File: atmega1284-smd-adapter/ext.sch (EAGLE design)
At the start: 5 parts

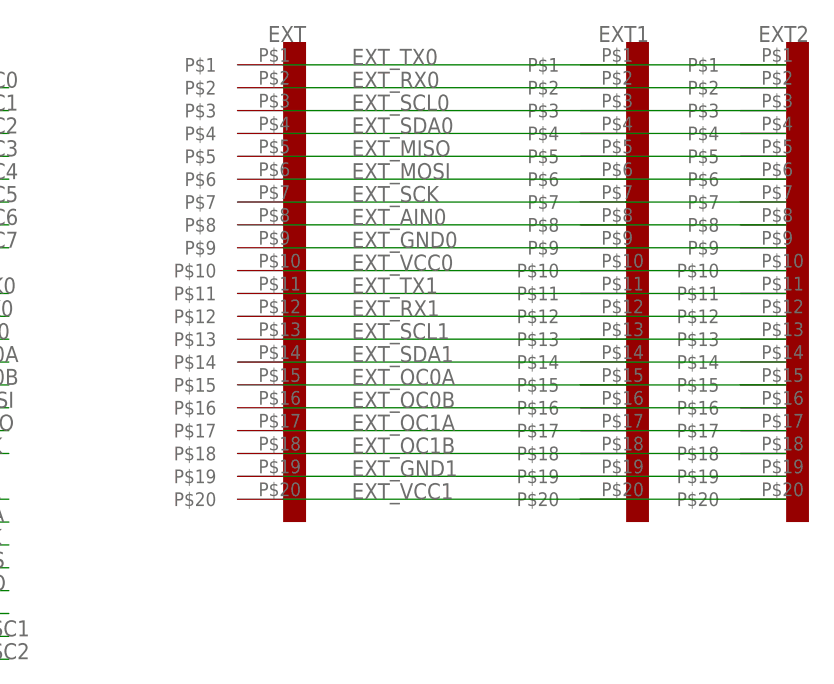
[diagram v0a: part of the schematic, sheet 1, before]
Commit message: [mk2 adapter split]
	- split the mk2-ext adapters into the actual mk2 extension board and
	  the atmega1284 smd adapter
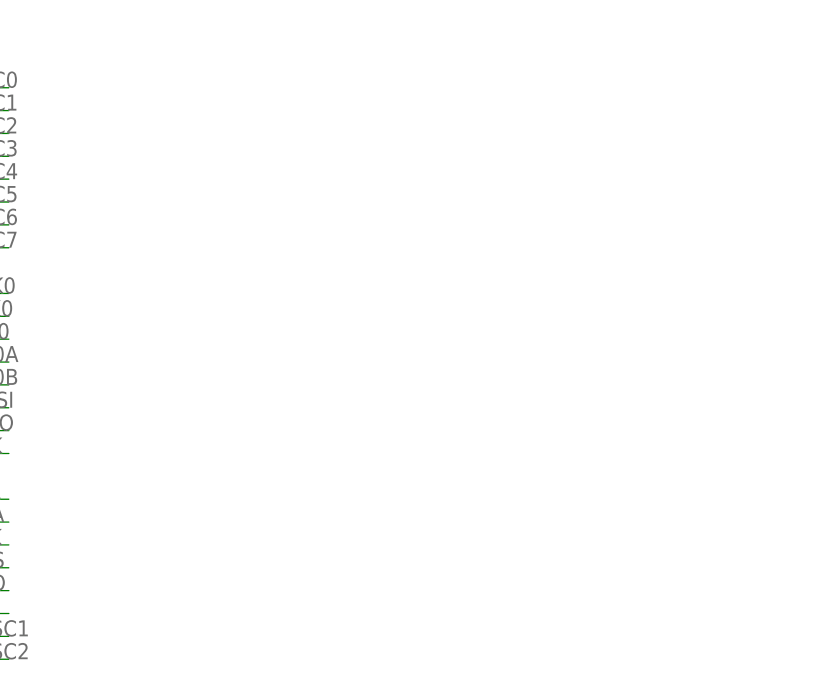
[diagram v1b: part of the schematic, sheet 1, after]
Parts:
- removed EXT, EXT1, EXT2: CON_DIL_20, connector:CON_DIL_20
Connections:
- removed net EXT_AIN0: EXT.P$8, EXT1.P$8, EXT2.P$8
- removed net EXT_GND0: EXT.P$9, EXT1.P$9, EXT2.P$9
- removed net EXT_GND1: EXT.P$19, EXT1.P$19, EXT2.P$19
- removed net EXT_MISO: EXT.P$5, EXT1.P$5, EXT2.P$5
- removed net EXT_MOSI: EXT.P$6, EXT1.P$6, EXT2.P$6
- removed net EXT_OC0A: EXT.P$15, EXT1.P$15, EXT2.P$15
- removed net EXT_OC0B: EXT.P$16, EXT1.P$16, EXT2.P$16
- removed net EXT_OC1A: EXT.P$17, EXT1.P$17, EXT2.P$17
- removed net EXT_OC1B: EXT.P$18, EXT1.P$18, EXT2.P$18
- removed net EXT_RX0: EXT.P$2, EXT1.P$2, EXT2.P$2
- removed net EXT_RX1: EXT.P$12, EXT1.P$12, EXT2.P$12
- removed net EXT_SCK: EXT.P$7, EXT1.P$7, EXT2.P$7
- removed net EXT_SCL0: EXT.P$3, EXT1.P$3, EXT2.P$3
- removed net EXT_SCL1: EXT.P$13, EXT1.P$13, EXT2.P$13
- removed net EXT_SDA0: EXT.P$4, EXT1.P$4, EXT2.P$4
- removed net EXT_SDA1: EXT.P$14, EXT1.P$14, EXT2.P$14
- removed net EXT_TX0: EXT.P$1, EXT1.P$1, EXT2.P$1
- removed net EXT_TX1: EXT.P$11, EXT1.P$11, EXT2.P$11
- removed net EXT_VCC0: EXT.P$10, EXT1.P$10, EXT2.P$10
- removed net EXT_VCC1: EXT.P$20, EXT1.P$20, EXT2.P$20
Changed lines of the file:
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@@
 <part name="GND7" library="supply1" library_urn="urn:adsk.eagle:library:371" deviceset="GND" device=""/>
 <part name="P+5" library="supply1" library_urn="urn:adsk.eagle:library:371" deviceset="VCC" device=""/>
-<part name="EXT" library="connector" deviceset="CON_DIL_20" device=""/>
 <part name="P+1" library="supply1" library_urn="urn:adsk.eagle:library:371" deviceset="VCC" device=""/>
 <part name="GND1" library="supply1" library_urn="urn:adsk.eagle:library:371" deviceset="GND" device=""/>
-<part name="EXT1" library="connector" deviceset="CON_DIL_20" device=""/>
-<part name="EXT2" library="connector" deviceset="CON_DIL_20" device=""/>
 </parts>
 <sheets>
@@
 <attribute name="VALUE" x="58.42" y="132.08" size="1.778" layer="96"/>
 </instance>
-<instance part="EXT" gate="G$1" x="152.4" y="109.22" smashed="yes">
-<attribute name="NAME" x="154.94" y="132.08" size="1.778" layer="95" rot="MR0"/>
-</instance>
 <instance part="P+1" gate="VCC" x="-33.02" y="132.08" smashed="yes">
 <attribute name="VALUE" x="-30.48" y="129.54" size="1.778" layer="96"/>
@@
 <instance part="GND1" gate="1" x="-30.48" y="30.48" smashed="yes">
 <attribute name="VALUE" x="-33.02" y="27.94" size="1.778" layer="96"/>
-</instance>
-<instance part="EXT1" gate="G$1" x="190.5" y="109.22" smashed="yes">
-<attribute name="NAME" x="193.04" y="132.08" size="1.778" layer="95" rot="MR0"/>
-</instance>
-<instance part="EXT2" gate="G$1" x="208.28" y="109.22" smashed="yes">
-<attribute name="NAME" x="210.82" y="132.08" size="1.778" layer="95" rot="MR0"/>
 </instance>
 </instances>
@@
 </segment>
 </net>
-<net name="EXT_TX0" class="0">
-<segment>
-<pinref part="EXT" gate="G$1" pin="P$1"/>
-<label x="160.02" y="129.54" size="1.778" layer="95"/>
-<wire x1="190.5" y1="129.54" x2="152.4" y2="129.54" width="0.1524" layer="91"/>
-<pinref part="EXT1" gate="G$1" pin="P$1"/>
-<pinref part="EXT2" gate="G$1" pin="P$1"/>
-<wire x1="208.28" y1="129.54" x2="190.5" y2="129.54" width="0.1524" layer="91"/>
-</segment>
-</net>
-<net name="EXT_RX0" class="0">
-<segment>
-<pinref part="EXT" gate="G$1" pin="P$2"/>
-<label x="160.02" y="127" size="1.778" layer="95"/>
-<wire x1="190.5" y1="127" x2="152.4" y2="127" width="0.1524" layer="91"/>
-<pinref part="EXT1" gate="G$1" pin="P$2"/>
-<pinref part="EXT2" gate="G$1" pin="P$2"/>
-<wire x1="208.28" y1="127" x2="190.5" y2="127" width="0.1524" layer="91"/>
-</segment>
-</net>
-<net name="EXT_SCL1" class="0">
-<segment>
-<pinref part="EXT" gate="G$1" pin="P$13"/>
-<label x="160.02" y="99.06" size="1.778" layer="95"/>
-<wire x1="190.5" y1="99.06" x2="152.4" y2="99.06" width="0.1524" layer="91"/>
-<pinref part="EXT1" gate="G$1" pin="P$13"/>
-<pinref part="EXT2" gate="G$1" pin="P$13"/>
-<wire x1="208.28" y1="99.06" x2="190.5" y2="99.06" width="0.1524" layer="91"/>
-</segment>
-</net>
-<net name="EXT_SDA0" class="0">
-<segment>
-<pinref part="EXT" gate="G$1" pin="P$4"/>
-<label x="160.02" y="121.92" size="1.778" layer="95"/>
-<wire x1="190.5" y1="121.92" x2="152.4" y2="121.92" width="0.1524" layer="91"/>
-<pinref part="EXT1" gate="G$1" pin="P$4"/>
-<pinref part="EXT2" gate="G$1" pin="P$4"/>
-<wire x1="208.28" y1="121.92" x2="190.5" y2="121.92" width="0.1524" layer="91"/>
-</segment>
-</net>
-<net name="EXT_MISO" class="0">
-<segment>
-<pinref part="EXT" gate="G$1" pin="P$5"/>
-<label x="160.02" y="119.38" size="1.778" layer="95"/>
-<wire x1="190.5" y1="119.38" x2="152.4" y2="119.38" width="0.1524" layer="91"/>
-<pinref part="EXT1" gate="G$1" pin="P$5"/>
-<pinref part="EXT2" gate="G$1" pin="P$5"/>
-<wire x1="208.28" y1="119.38" x2="190.5" y2="119.38" width="0.1524" layer="91"/>
-</segment>
-</net>
-<net name="EXT_MOSI" class="0">
-<segment>
-<pinref part="EXT" gate="G$1" pin="P$6"/>
-<label x="160.02" y="116.84" size="1.778" layer="95"/>
-<wire x1="190.5" y1="116.84" x2="152.4" y2="116.84" width="0.1524" layer="91"/>
-<pinref part="EXT1" gate="G$1" pin="P$6"/>
-<pinref part="EXT2" gate="G$1" pin="P$6"/>
-<wire x1="208.28" y1="116.84" x2="190.5" y2="116.84" width="0.1524" layer="91"/>
-</segment>
-</net>
-<net name="EXT_SCK" class="0">
-<segment>
-<pinref part="EXT" gate="G$1" pin="P$7"/>
-<label x="160.02" y="114.3" size="1.778" layer="95"/>
-<wire x1="190.5" y1="114.3" x2="152.4" y2="114.3" width="0.1524" layer="91"/>
-<pinref part="EXT1" gate="G$1" pin="P$7"/>
-<pinref part="EXT2" gate="G$1" pin="P$7"/>
-<wire x1="208.28" y1="114.3" x2="190.5" y2="114.3" width="0.1524" layer="91"/>
-</segment>
-</net>
-<net name="EXT_AIN0" class="0">
-<segment>
-<pinref part="EXT" gate="G$1" pin="P$8"/>
-<label x="160.02" y="111.76" size="1.778" layer="95"/>
-<wire x1="190.5" y1="111.76" x2="152.4" y2="111.76" width="0.1524" layer="91"/>
-<pinref part="EXT1" gate="G$1" pin="P$8"/>
-<pinref part="EXT2" gate="G$1" pin="P$8"/>
-<wire x1="208.28" y1="111.76" x2="190.5" y2="111.76" width="0.1524" layer="91"/>
-</segment>
-</net>
-<net name="EXT_GND0" class="0">
-<segment>
-<pinref part="EXT" gate="G$1" pin="P$9"/>
-<label x="160.02" y="109.22" size="1.778" layer="95"/>
-<wire x1="190.5" y1="109.22" x2="152.4" y2="109.22" width="0.1524" layer="91"/>
-<pinref part="EXT1" gate="G$1" pin="P$9"/>
-<pinref part="EXT2" gate="G$1" pin="P$9"/>
-<wire x1="208.28" y1="109.22" x2="190.5" y2="109.22" width="0.1524" layer="91"/>
-</segment>
-</net>
-<net name="EXT_VCC0" class="0">
-<segment>
-<pinref part="EXT" gate="G$1" pin="P$10"/>
-<label x="160.02" y="106.68" size="1.778" layer="95"/>
-<wire x1="190.5" y1="106.68" x2="152.4" y2="106.68" width="0.1524" layer="91"/>
-<pinref part="EXT1" gate="G$1" pin="P$10"/>
-<pinref part="EXT2" gate="G$1" pin="P$10"/>
-<wire x1="208.28" y1="106.68" x2="190.5" y2="106.68" width="0.1524" layer="91"/>
-</segment>
-</net>
-<net name="EXT_TX1" class="0">
-<segment>
-<pinref part="EXT" gate="G$1" pin="P$11"/>
-<label x="160.02" y="104.14" size="1.778" layer="95"/>
-<wire x1="190.5" y1="104.14" x2="152.4" y2="104.14" width="0.1524" layer="91"/>
-<pinref part="EXT1" gate="G$1" pin="P$11"/>
-<pinref part="EXT2" gate="G$1" pin="P$11"/>
-<wire x1="208.28" y1="104.14" x2="190.5" y2="104.14" width="0.1524" layer="91"/>
-</segment>
-</net>
-<net name="EXT_RX1" class="0">
-<segment>
-<pinref part="EXT" gate="G$1" pin="P$12"/>
-<label x="160.02" y="101.6" size="1.778" layer="95"/>
-<wire x1="190.5" y1="101.6" x2="152.4" y2="101.6" width="0.1524" layer="91"/>
-<pinref part="EXT1" gate="G$1" pin="P$12"/>
-<pinref part="EXT2" gate="G$1" pin="P$12"/>
-<wire x1="208.28" y1="101.6" x2="190.5" y2="101.6" width="0.1524" layer="91"/>
-</segment>
-</net>
-<net name="EXT_SCL0" class="0">
-<segment>
-<pinref part="EXT" gate="G$1" pin="P$3"/>
-<label x="160.02" y="124.46" size="1.778" layer="95"/>
-<wire x1="190.5" y1="124.46" x2="152.4" y2="124.46" width="0.1524" layer="91"/>
-<pinref part="EXT1" gate="G$1" pin="P$3"/>
-<pinref part="EXT2" gate="G$1" pin="P$3"/>
-<wire x1="208.28" y1="124.46" x2="190.5" y2="124.46" width="0.1524" layer="91"/>
-</segment>
-</net>
-<net name="EXT_SDA1" class="0">
-<segment>
-<pinref part="EXT" gate="G$1" pin="P$14"/>
-<label x="160.02" y="96.52" size="1.778" layer="95"/>
-<wire x1="190.5" y1="96.52" x2="152.4" y2="96.52" width="0.1524" layer="91"/>
-<pinref part="EXT1" gate="G$1" pin="P$14"/>
-<pinref part="EXT2" gate="G$1" pin="P$14"/>
-<wire x1="208.28" y1="96.52" x2="190.5" y2="96.52" width="0.1524" layer="91"/>
-</segment>
-</net>
-<net name="EXT_OC0A" class="0">
-<segment>
-<pinref part="EXT" gate="G$1" pin="P$15"/>
-<label x="160.02" y="93.98" size="1.778" layer="95"/>
-<wire x1="190.5" y1="93.98" x2="152.4" y2="93.98" width="0.1524" layer="91"/>
-<pinref part="EXT1" gate="G$1" pin="P$15"/>
-<pinref part="EXT2" gate="G$1" pin="P$15"/>
-<wire x1="208.28" y1="93.98" x2="190.5" y2="93.98" width="0.1524" layer="91"/>
-</segment>
-</net>
-<net name="EXT_OC0B" class="0">
-<segment>
-<pinref part="EXT" gate="G$1" pin="P$16"/>
-<label x="160.02" y="91.44" size="1.778" layer="95"/>
-<wire x1="190.5" y1="91.44" x2="152.4" y2="91.44" width="0.1524" layer="91"/>
-<pinref part="EXT1" gate="G$1" pin="P$16"/>
-<pinref part="EXT2" gate="G$1" pin="P$16"/>
-<wire x1="208.28" y1="91.44" x2="190.5" y2="91.44" width="0.1524" layer="91"/>
-</segment>
-</net>
-<net name="EXT_OC1A" class="0">
-<segment>
-<pinref part="EXT" gate="G$1" pin="P$17"/>
-<label x="160.02" y="88.9" size="1.778" layer="95"/>
-<wire x1="190.5" y1="88.9" x2="152.4" y2="88.9" width="0.1524" layer="91"/>
-<pinref part="EXT1" gate="G$1" pin="P$17"/>
-<pinref part="EXT2" gate="G$1" pin="P$17"/>
-<wire x1="208.28" y1="88.9" x2="190.5" y2="88.9" width="0.1524" layer="91"/>
-</segment>
-</net>
-<net name="EXT_OC1B" class="0">
-<segment>
-<pinref part="EXT" gate="G$1" pin="P$18"/>
-<label x="160.02" y="86.36" size="1.778" layer="95"/>
-<wire x1="190.5" y1="86.36" x2="152.4" y2="86.36" width="0.1524" layer="91"/>
-<pinref part="EXT1" gate="G$1" pin="P$18"/>
-<pinref part="EXT2" gate="G$1" pin="P$18"/>
-<wire x1="208.28" y1="86.36" x2="190.5" y2="86.36" width="0.1524" layer="91"/>
-</segment>
-</net>
-<net name="EXT_GND1" class="0">
-<segment>
-<pinref part="EXT" gate="G$1" pin="P$19"/>
-<label x="160.02" y="83.82" size="1.778" layer="95"/>
-<wire x1="190.5" y1="83.82" x2="152.4" y2="83.82" width="0.1524" layer="91"/>
-<pinref part="EXT1" gate="G$1" pin="P$19"/>
-<pinref part="EXT2" gate="G$1" pin="P$19"/>
-<wire x1="208.28" y1="83.82" x2="190.5" y2="83.82" width="0.1524" layer="91"/>
-</segment>
-</net>
-<net name="EXT_VCC1" class="0">
-<segment>
-<pinref part="EXT" gate="G$1" pin="P$20"/>
-<label x="160.02" y="81.28" size="1.778" layer="95"/>
-<wire x1="190.5" y1="81.28" x2="152.4" y2="81.28" width="0.1524" layer="91"/>
-<pinref part="EXT1" gate="G$1" pin="P$20"/>
-<pinref part="EXT2" gate="G$1" pin="P$20"/>
-<wire x1="208.28" y1="81.28" x2="190.5" y2="81.28" width="0.1524" layer="91"/>
-</segment>
-</net>

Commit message: [fix atmega1284p adapter drill size]
	- extend the drill size of the atmega1284p adapter
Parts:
- U$3: device 1284p.rpt:MEGA1284P_ADAPTER -> mega1284p:MEGA1284P_ADAPTER
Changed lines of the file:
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@@
 <parts>
 <part name="U$1" library="1284p.rpt" deviceset="MEGA1284P_TQFP" device=""/>
-<part name="U$3" library="1284p.rpt" deviceset="MEGA1284P_ADAPTER" device=""/>
+<part name="U$3" library="mega1284p" deviceset="MEGA1284P_ADAPTER" device=""/>
 <part name="GND7" library="supply1" library_urn="urn:adsk.eagle:library:371" deviceset="GND" device=""/>
 <part name="P+5" library="supply1" library_urn="urn:adsk.eagle:library:371" deviceset="VCC" device=""/>
